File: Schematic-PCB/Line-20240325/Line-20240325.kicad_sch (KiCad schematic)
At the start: 138 parts, among them J1 Conn_01x02_Pin, J2 Conn_01x04_Pin, J3 USB_C_Receptacle_USB2.0_16P, SW1 SW_Push, U33 ATmega2560-16A, U34 CH340E, Y1 16MHz

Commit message: ラインセンサ基板のPCBを更新
ちょっと停滞中... ヘルプ求む、
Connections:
- net line33: no longer names the net of U33.51 (PG0/D41)
- net line34: no longer names the net of U33.52 (PG1/D40)
- net line35: no longer names the net of U33.70 (PG2/D39)
- no-connect marks 46 -> 49
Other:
- moved on the sheet: C1, C2, C3, C4, C6, C7, C8, C9, D33, D37, F1, J1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

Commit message: ミラーの3Dモデルを追加、ライン基板のPCB更新
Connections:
- net at U3.1 (Emitter): now also Comp1.2 (IN1-); no longer Comp1.6 (IN2-)
- net at U4.1 (Emitter): now also Comp1.6 (IN2-); no longer Comp1.2 (IN1-)
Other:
- moved on the sheet: U3, U4
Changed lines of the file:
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@@
 	(symbol
 		(lib_id "@2024-Line:NJL7502L")
-		(at 62.23 55.88 180)
+		(at 62.23 40.64 180)
 		(unit 1)
 		(exclude_from_sim no)
@@
 		(dnp no)
 		(property "Reference" "U3"
-			(at 62.23 49.53 0)
+			(at 62.23 34.29 0)
 			(effects
 				(font
@@
 		)
 		(property "Value" "~"
-			(at 62.23 49.53 0)
+			(at 62.23 34.29 0)
 			(effects
 				(font
@@
 		)
 		(property "Footprint" "@2024-Line:NJL7502L"
-			(at 62.23 59.69 0)
+			(at 62.23 44.45 0)
 			(effects
 				(font
@@
 		)
 		(property "Datasheet" ""
-			(at 62.23 59.69 0)
+			(at 62.23 44.45 0)
 			(effects
 				(font
@@
 		)
 		(property "Description" ""
-			(at 62.23 55.88 0)
+			(at 62.23 40.64 0)
 			(effects
 				(font
@@
 	(symbol
 		(lib_id "@2024-Line:NJL7502L")
-		(at 62.23 40.64 180)
+		(at 62.23 55.88 180)
 		(unit 1)
 		(exclude_from_sim no)
@@
 		(dnp no)
 		(property "Reference" "U4"
-			(at 62.23 34.29 0)
+			(at 62.23 49.53 0)
 			(effects
 				(font
@@
 		)
 		(property "Value" "~"
-			(at 62.23 34.29 0)
+			(at 62.23 49.53 0)
 			(effects
 				(font
@@
 		)
 		(property "Footprint" "@2024-Line:NJL7502L"
-			(at 62.23 44.45 0)
+			(at 62.23 59.69 0)
 			(effects
 				(font
@@
 		)
 		(property "Datasheet" ""
-			(at 62.23 44.45 0)
+			(at 62.23 59.69 0)
 			(effects
 				(font
@@
 		)
 		(property "Description" ""
-			(at 62.23 40.64 0)
-			(effects
-				(font
+			(at 62.23 55.88 0)
+			(effects
+				(font

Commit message: ラインセンサのPCBを更新した
主にフォトトランジスタ・コンパレータ周りを配線した
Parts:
- R42, R43: value 10K -> 1K
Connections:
- net line01: now also U33.12 (PH0/D17/RX2); no longer U33.78 (PA0/D22)
- net line02: now also U33.13 (PH1/D16/TX2); no longer U33.77 (PA1/D23)
- net line03: now also U33.14 (PH2); no longer U33.76 (PA2/D24)
- net line04: now also U33.15 (PH3/D6); no longer U33.75 (PA3/D25)
- net line05: now also Comp2.8 (OUT3), U33.16 (PH4/D7); no longer Comp2.14 (OUT4), U33.74 (PA4/D26)
- net line06: now also Comp2.14 (OUT4), U33.17 (PH5/D8); no longer Comp2.8 (OUT3), U33.73 (PA5/D27)
- net line07: now also Comp2.7 (OUT2), U33.18 (PH6/D9); no longer Comp2.1 (OUT1), U33.72 (PA6/D28)
- net line08: now also Comp2.1 (OUT1), U33.19 (PB0/D53/SS); no longer Comp2.7 (OUT2), U33.71 (PA7/D29)
- net line09: now also U33.26 (PB7/D13); no longer U33.19 (PB0/D53/SS)
- net line10: now also U33.27 (PH7); no longer U33.20 (PB1/D52/SCK)
- net line11: now also U33.28 (PG3); no longer U33.21 (PB2/D51/MOSI)
- net line12: now also U33.29 (PG4); no longer U33.22 (PB3/D50/MISO)
- net line13: now also U33.51 (PG0/D41); no longer U33.23 (PB4/D10)
- net line14: now also U33.52 (PG1/D40); no longer U33.24 (PB5/D11)
- net line15: now also U33.53 (PC0/D37); no longer U33.25 (PB6/D12)
- net line16: now also U33.54 (PC1/D36); no longer U33.26 (PB7/D13)
- net line17: now also Comp5.8 (OUT3), U33.63 (PJ0/D15/RX3); no longer Comp5.14 (OUT4), U33.53 (PC0/D37)
- net line18: now also Comp5.14 (OUT4), U33.64 (PJ1/D14/TX3); no longer Comp5.8 (OUT3), U33.54 (PC1/D36)
- net line19: now also U33.65 (PJ2); no longer U33.55 (PC2/D35)
- net line20: now also U33.66 (PJ3); no longer U33.56 (PC3/D34)
- net line21: now also U33.20 (PB1/D52/SCK); no longer U33.57 (PC4/D33)
- net line22: now also U33.21 (PB2/D51/MOSI); no longer U33.58 (PC5/D32)
- net line23: now also U33.22 (PB3/D50/MISO); no longer U33.59 (PC6/D31)
- net line24: now also U33.23 (PB4/D10); no longer U33.60 (PC7/D30)
- net line25: now also U33.47 (PD4); no longer U33.97 (PF0/ADC0)
- net line26: now also U33.48 (PD5); no longer U33.96 (PF1/ADC1)
- net line27: now also U33.49 (PD6); no longer U33.95 (PF2/ADC2)
- net line28: now also U33.50 (PD7/D38); no longer U33.94 (PF3/ADC3)
- net line29: now also U33.55 (PC2/D35); no longer U33.93 (PF4/ADC4)
- net line30: now also U33.56 (PC3/D34); no longer U33.92 (PF5/ADC5)
- net line31: now also U33.57 (PC4/D33); no longer U33.91 (PF6/ADC6)
- net line32: now also U33.58 (PC5/D32); no longer U33.90 (PF7/ADC7)
- net at Comp2.13 (IN4-): now also U6.1 (Emitter); no longer U5.1 (Emitter)
- net at Comp2.2 (IN1-): now also U8.1 (Emitter); no longer U7.1 (Emitter)
- net at Comp2.6 (IN2-): now also U7.1 (Emitter); no longer U8.1 (Emitter)
- net at Comp2.9 (IN3-): now also U5.1 (Emitter); no longer U6.1 (Emitter)
- net at R36.2: now also U33.36 (PL1/D48); no longer U33.16 (PH4/D7)
- net at U17.1 (Emitter): now also Comp5.9 (IN3-); no longer Comp5.13 (IN4-)
- net at R39.2: now also U33.35 (PL0/D49); no longer U33.15 (PH3/D6)
- net at R35.2: now also U33.37 (PL2/D47); no longer U33.17 (PH5/D8)
- net at U18.1 (Emitter): now also Comp5.13 (IN4-); no longer Comp5.9 (IN3-)
- no-connect marks 49 -> 29
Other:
- moved on the sheet: C5, D34, D35, D36, R34, R35, R36, R39, U17, U18, U5, U6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

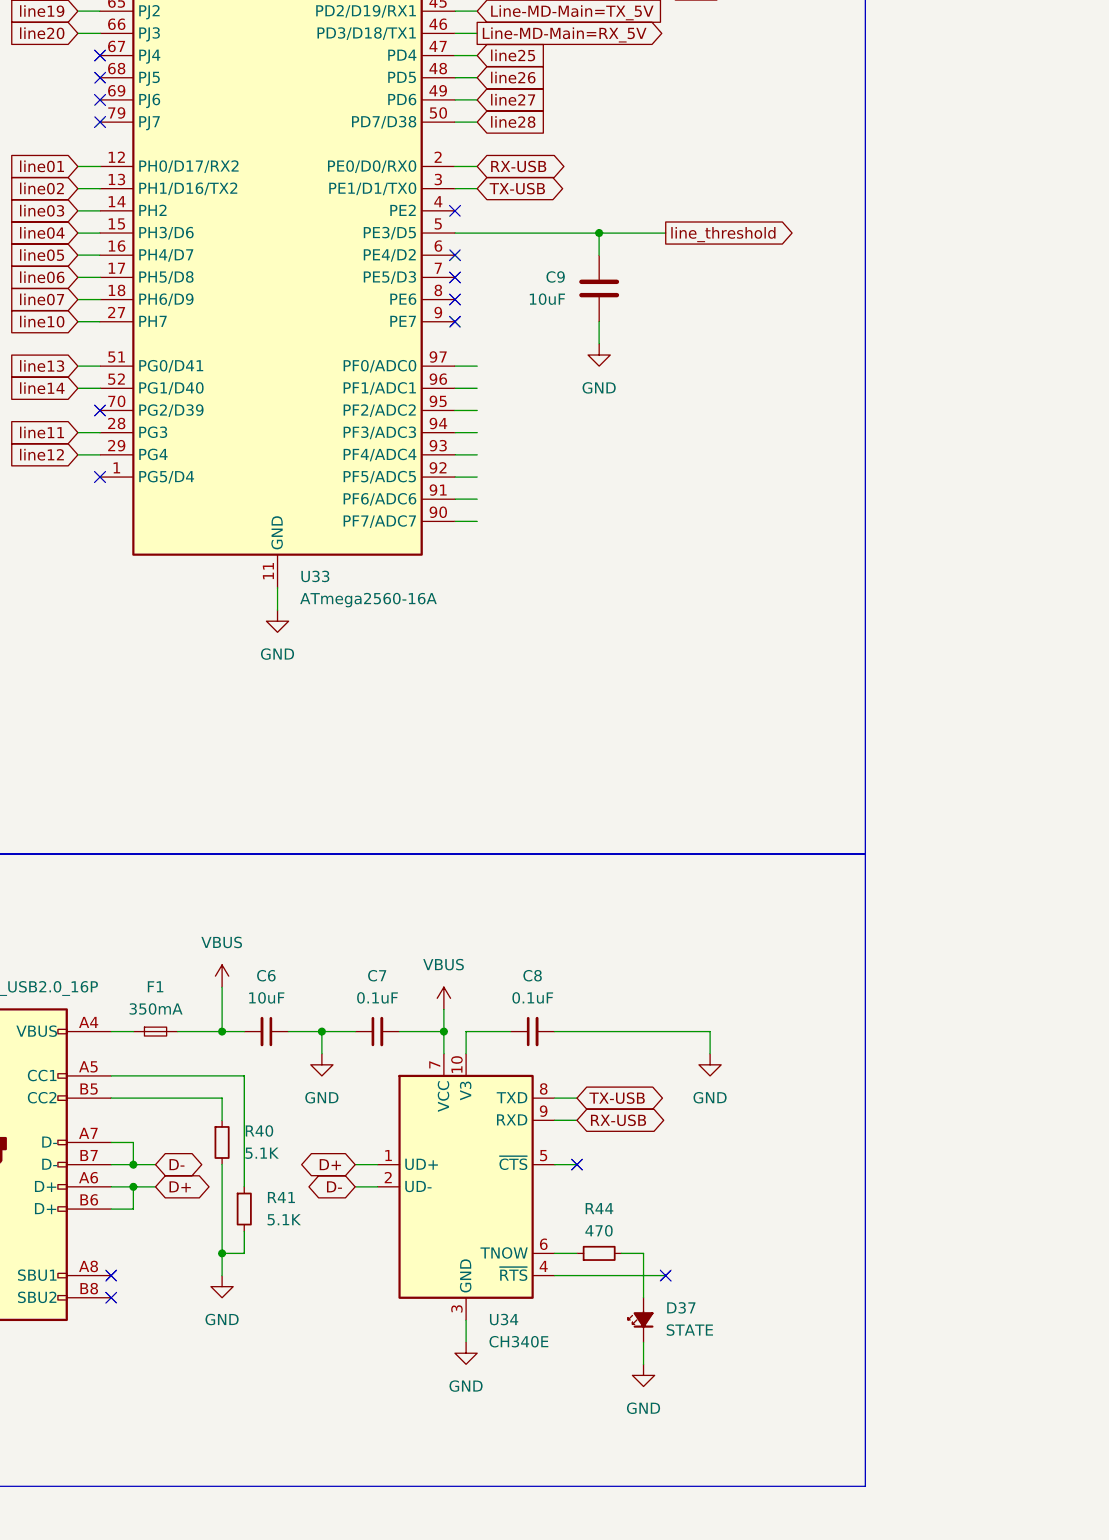
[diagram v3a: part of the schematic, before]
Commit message: 山本さんのアドバイスを参考に回路図を更新した
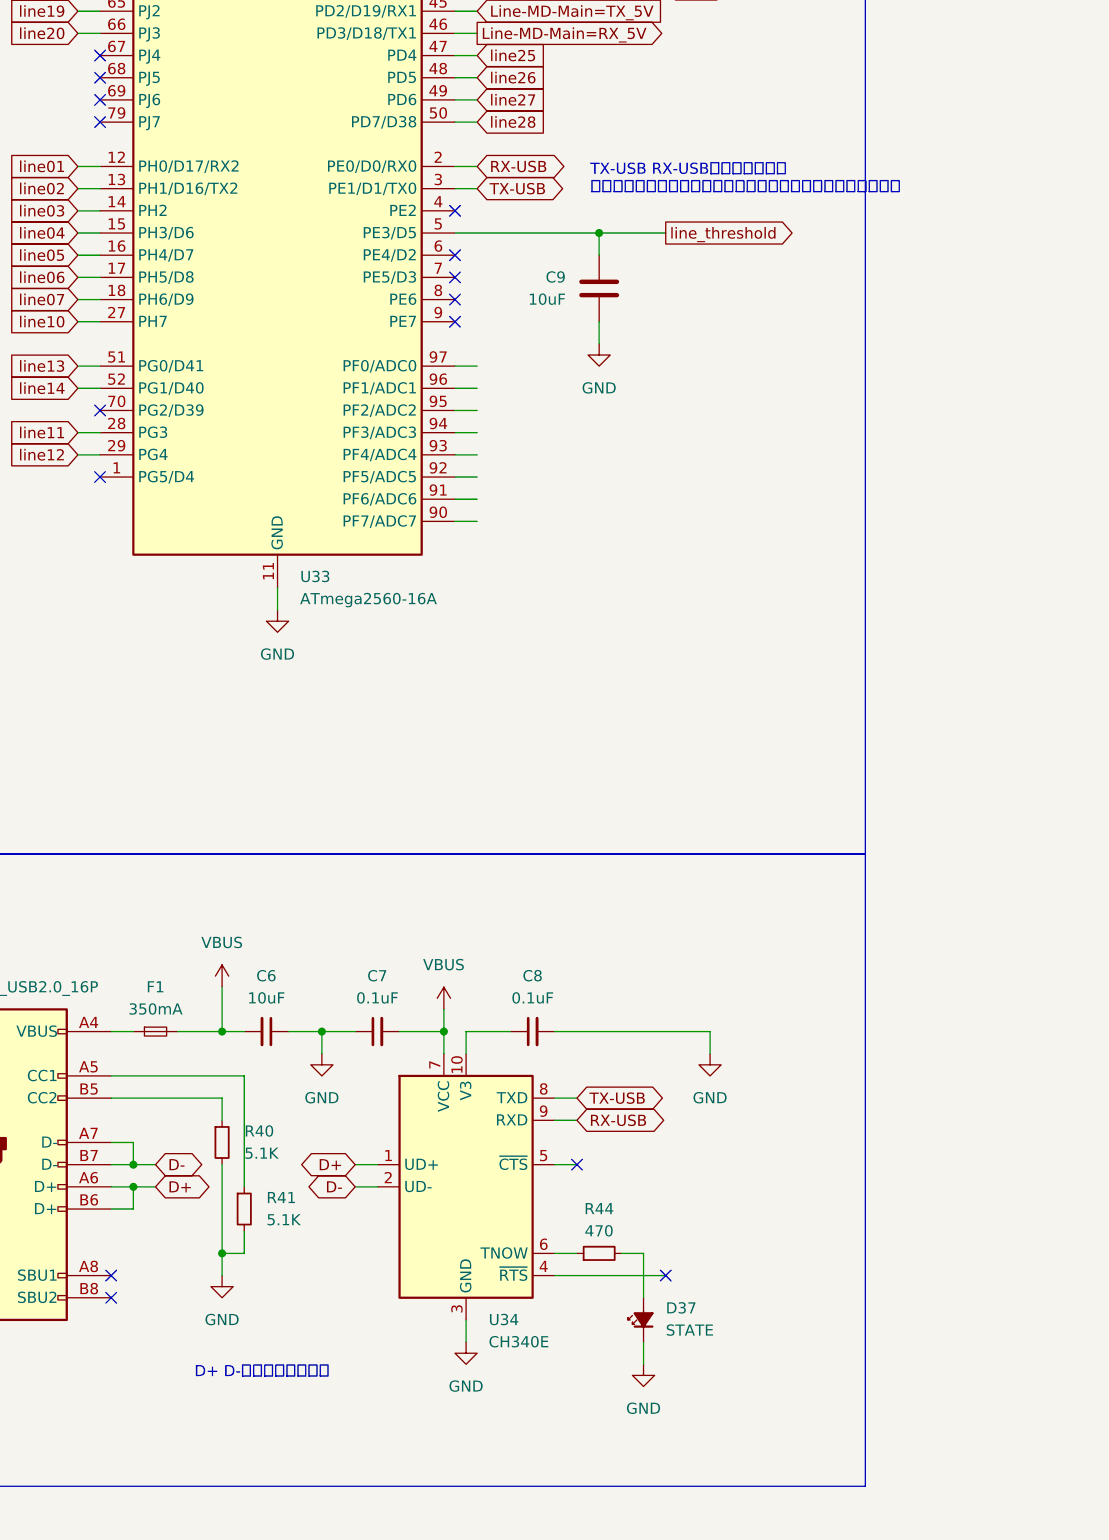
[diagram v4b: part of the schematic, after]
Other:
- note added: "D+ D-間は短く配線する"
- note added: "TX-USB RX-USBの配線の間に、 ノイズ対策用の抵抗を入れられるようにパターンを作っておく"
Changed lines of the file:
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@@
+		)
+	)
+	(text "TX-USB RX-USBの配線の間に、\nノイズ対策用の抵抗を入れられるようにパターンを作っておく"
+		(exclude_from_sim no)
+		(at 269.494 148.844 0)
+		(effects
+			(font
+				(size 1.27 1.27)
+			)
+			(justify left)
 		)
 	)
@@
 		)
 	)
+	(text "D+ D-間は短く配線する\n"
+		(exclude_from_sim no)
+		(at 231.902 285.496 0)
+		(effects
+			(font
+				(size 1.27 1.27)
+			)
+		)
+	)

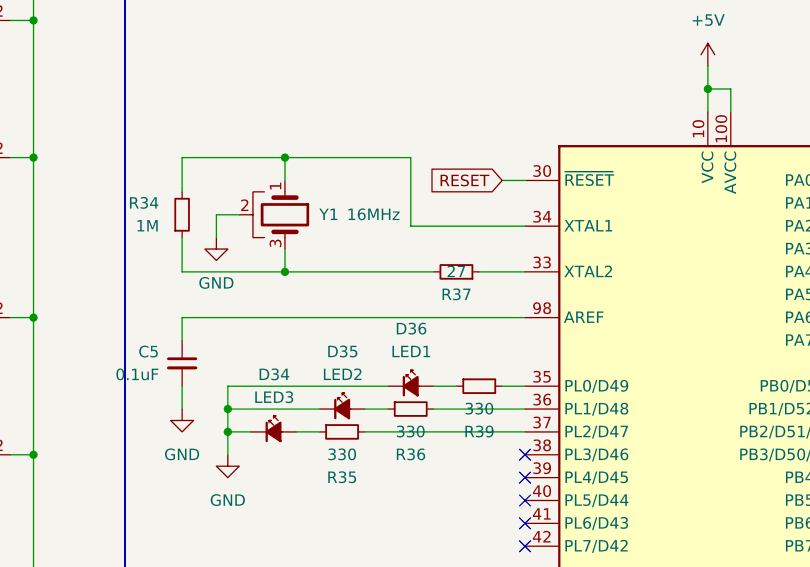
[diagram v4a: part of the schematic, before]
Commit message: ラインセンサのPCBを更新した
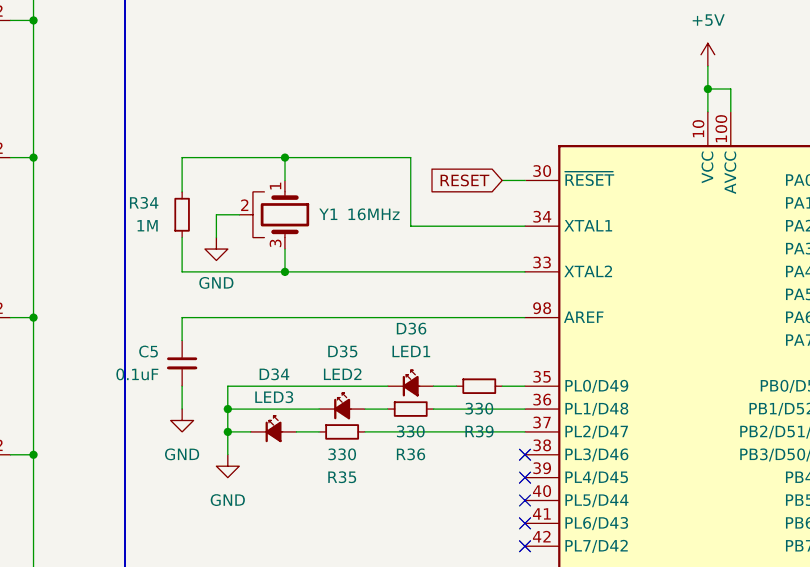
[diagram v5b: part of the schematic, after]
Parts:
- removed R37: 27, Resistor_SMD:R_0603_1608Metric, symbol Device:R_Small
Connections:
- net at U33.33 (XTAL2): now also R34.1, Y1.3
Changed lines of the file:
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@@
 	(wire
 		(pts
-			(xy 208.28 66.04) (xy 213.36 66.04)
-		)
-		(stroke
-			(width 0)
-			(type default)
-		)
-	)
-	(wire
-		(pts
 			(xy 110.49 316.23) (xy 110.49 313.69)
 		)
@@
 	(wire
 		(pts
-			(xy 186.69 66.04) (xy 203.2 66.04)
+			(xy 186.69 66.04) (xy 213.36 66.04)
 		)
 		(stroke
@@
 			)
 		)
-	)
-	(symbol
-		(lib_id "Device:R_Small")
-		(at 205.74 66.04 270)
-		(mirror x)
-		(unit 1)
-		(exclude_from_sim no)
-		(in_bom yes)
-		(on_board yes)
-		(dnp no)
-		(property "Reference" "R37"
-			(at 205.74 68.58 90)
-			(effects
-				(font
-					(size 1.27 1.27)
-				)
-			)
-		)
-		(property "Value" "27"
-			(at 205.74 66.04 90)
-			(effects
-				(font
-					(size 1.27 1.27)
-				)
-			)
-		)
-		(property "Footprint" "Resistor_SMD:R_0603_1608Metric"
-			(at 205.74 66.04 0)
-			(effects
-				(font
-					(size 1.27 1.27)
-				)
-				(hide yes)
-			)
-		)
-		(property "Datasheet" "~"
-			(at 205.74 66.04 0)
-			(effects
-				(font
-					(size 1.27 1.27)
-				)
-				(hide yes)
-			)
-		)
-		(property "Description" "Resistor, small symbol"
-			(at 205.74 66.04 0)
-			(effects
-				(font
-					(size 1.27 1.27)
-				)
-				(hide yes)
-			)
-		)
-		(pin "1"
-		)
-		(pin "2"
-		)
-		(instances
-			(project "Line-20240325"
-				(path "/3ba7fdd5-fa74-4790-8511-1df233340313"
-					(reference "R37")
-					(unit 1)
-				)
-			)
-		)
